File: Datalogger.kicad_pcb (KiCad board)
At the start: 2 copper layers, 122.2 x 99.6 mm, 66 parts, among them J1 From Mains, J2 AVR-ISP-6, J3 USB_B, J4 Screw, J5 Screw, J6 Screw, J7 Screw, J8 Conn_01x04_Socket, Q1 BC547, Q2 BC847, Q3 BC847, Q4 TIP127, U1 AMS1117-3.3, U2 LM2596T-5, U3 ATmega2560-16A, U4 PC817, U5 PC817, U6 PC817, U7 CNY74-4H, Y1 16MHz

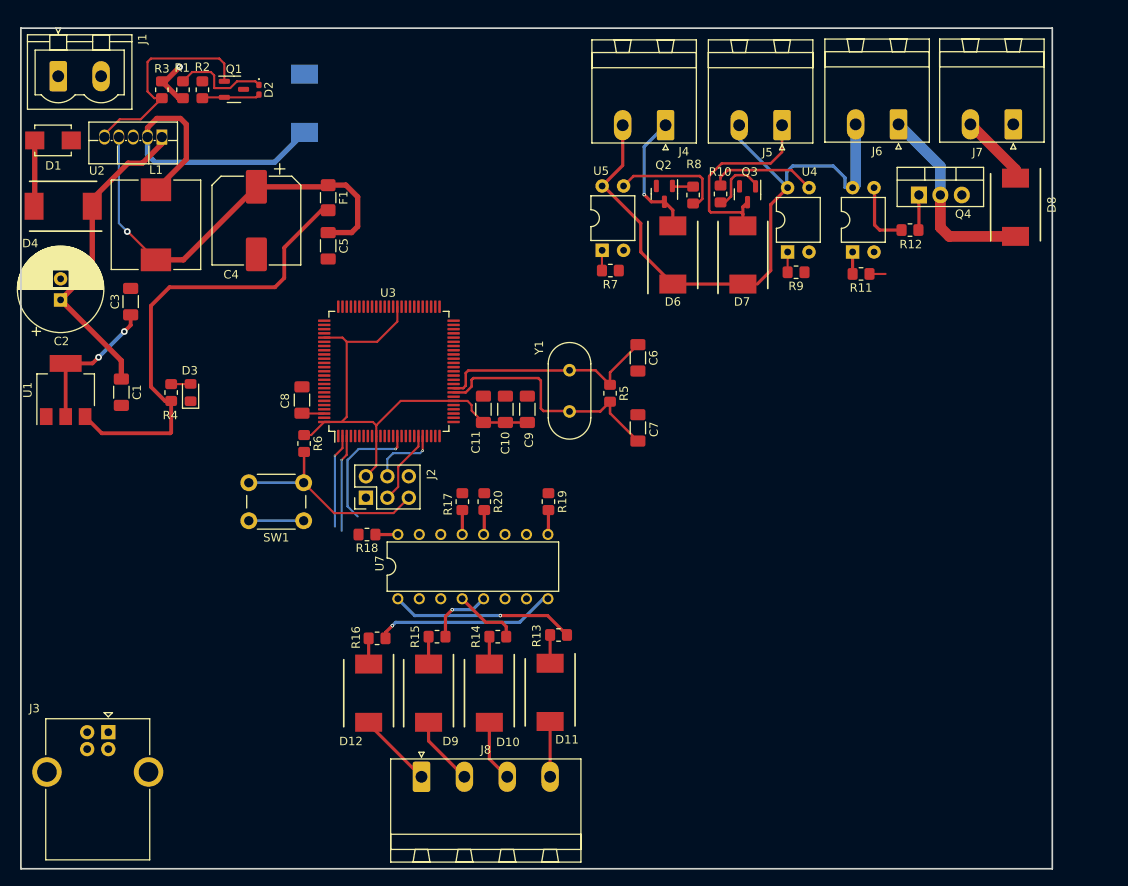
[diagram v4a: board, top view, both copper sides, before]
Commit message: Schematic of 4-20mA sensor
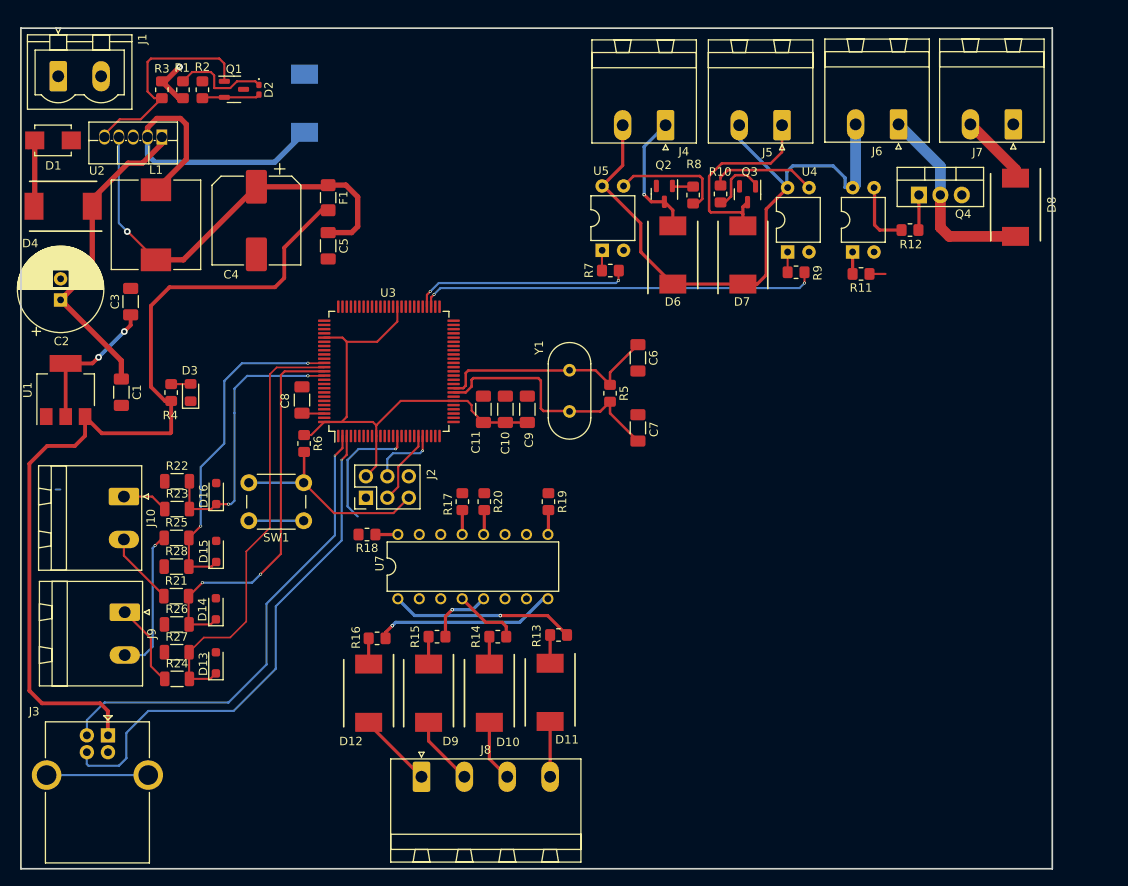
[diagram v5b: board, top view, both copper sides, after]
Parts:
- added D13: 5V, Diode_SMD:D_SOD-323_HandSoldering, F.Cu at (104.4, 114.1)
- added D14: 5V, Diode_SMD:D_SOD-323_HandSoldering, F.Cu at (104.4, 107.7)
- added D15: 5V, Diode_SMD:D_SOD-323_HandSoldering, F.Cu at (104.4, 100.9)
- added D16: 5V, Diode_SMD:D_SOD-323_HandSoldering, F.Cu at (104.4, 94.0)
- added J10: Screw, Connector_Phoenix_MSTB:PhoenixContact_MSTBA_2,5_2-G-5,08_1x02_P5.08mm_Horizontal, F.Cu at (93.5, 94.4)
- added J9: Screw, Connector_Phoenix_MSTB:PhoenixContact_MSTBA_2,5_2-G-5,08_1x02_P5.08mm_Horizontal, F.Cu at (93.6, 108.1)
- added R21: 100k, Resistor_SMD:R_1206_3216Metric, F.Cu at (99.7, 106.2)
- added R22: 100k, Resistor_SMD:R_1206_3216Metric, F.Cu at (99.8, 92.6)
- added R23: 100k, Resistor_SMD:R_1206_3216Metric, F.Cu at (99.8, 95.9)
- added R24: 100k, Resistor_SMD:R_1206_3216Metric, F.Cu at (99.8, 116.0)
- added R25: 100k, Resistor_SMD:R_1206_3216Metric, F.Cu at (99.7, 99.3)
- added R26: 100k, Resistor_SMD:R_1206_3216Metric, F.Cu at (99.8, 109.5)
- added R27: 100k, Resistor_SMD:R_1206_3216Metric, F.Cu at (99.8, 112.8)
- added R28: 100k, Resistor_SMD:R_1206_3216Metric, F.Cu at (99.7, 102.7)
- moved J3 0.37 mm to (91.6, 122.7)
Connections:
- R17 pad 2: /Digital Pin/DIN3 -> /ATMEGA2560/DIN3
- R18 pad 2: /Digital Pin/DIN4 -> /ATMEGA2560/DIN4
- R19 pad 2: /Digital Pin/DIN1 -> /ATMEGA2560/DIN1
- R20 pad 2: /Digital Pin/DIN2 -> /ATMEGA2560/DIN2
- U3 pad 86: unconnected-(U3-PK3-Pad86) -> AIN3
- U3 pad 87: unconnected-(U3-PK2-Pad87) -> AIN2
- U3 pad 88: unconnected-(U3-PK1-Pad88) -> AIN1
- U3 pad 89: unconnected-(U3-PK0-Pad89) -> AIN0
- U7 pad 12: /Digital Pin/DIN2 -> /ATMEGA2560/DIN2
- U7 pad 13: /Digital Pin/DIN3 -> /ATMEGA2560/DIN3
- U7 pad 16: /Digital Pin/DIN4 -> /ATMEGA2560/DIN4
- U7 pad 9: /Digital Pin/DIN1 -> /ATMEGA2560/DIN1
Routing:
- net AIN2: track 0.00 -> 52.1 mm
- net +5V: track 115.2 -> 165.5 mm
- net PROG_TX0: track 11.5 -> 61.5 mm
- net /ATMEGA2560/Relay_1: track 0.14 -> 47.5 mm, vias 0 -> 2
- net AIN1: track 0.00 -> 46.3 mm, vias 0 -> 2
- net PROG_RX0: track 11.1 -> 56.6 mm
- net AIN3: track 0.00 -> 39.9 mm, vias 0 -> 2
- net AIN0: track 0.00 -> 33.6 mm, vias 0 -> 2
- net /ATMEGA2560/Relay_2: track 0.00 -> 26.0 mm, vias 0 -> 2
- net Net-(J9-Pin_2): track 0.00 -> 17.3 mm, vias 0 -> 1
- net unconnected-(J3-Shield-Pad5): track 0.00 -> 12.0 mm
- net Net-(J9-Pin_1): track 0.00 -> 9.94 mm
- net Net-(J10-Pin_2): track 0.00 -> 9.22 mm
- net Net-(J10-Pin_1): track 0.00 -> 5.79 mm
- net /Digital Pin/DIN2: track 2.92 -> 0.00 mm
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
